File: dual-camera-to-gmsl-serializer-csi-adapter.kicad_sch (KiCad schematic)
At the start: 120 parts, among them J1 Conn_FFC_WE_68715014022, J2 Conn_FFC_WE_68715014022, J3 Conn_FFC_WE_68715014022, U1 TPS2117DRLR, U2 TPS2117DRLR, U3 AP62301_TSOT

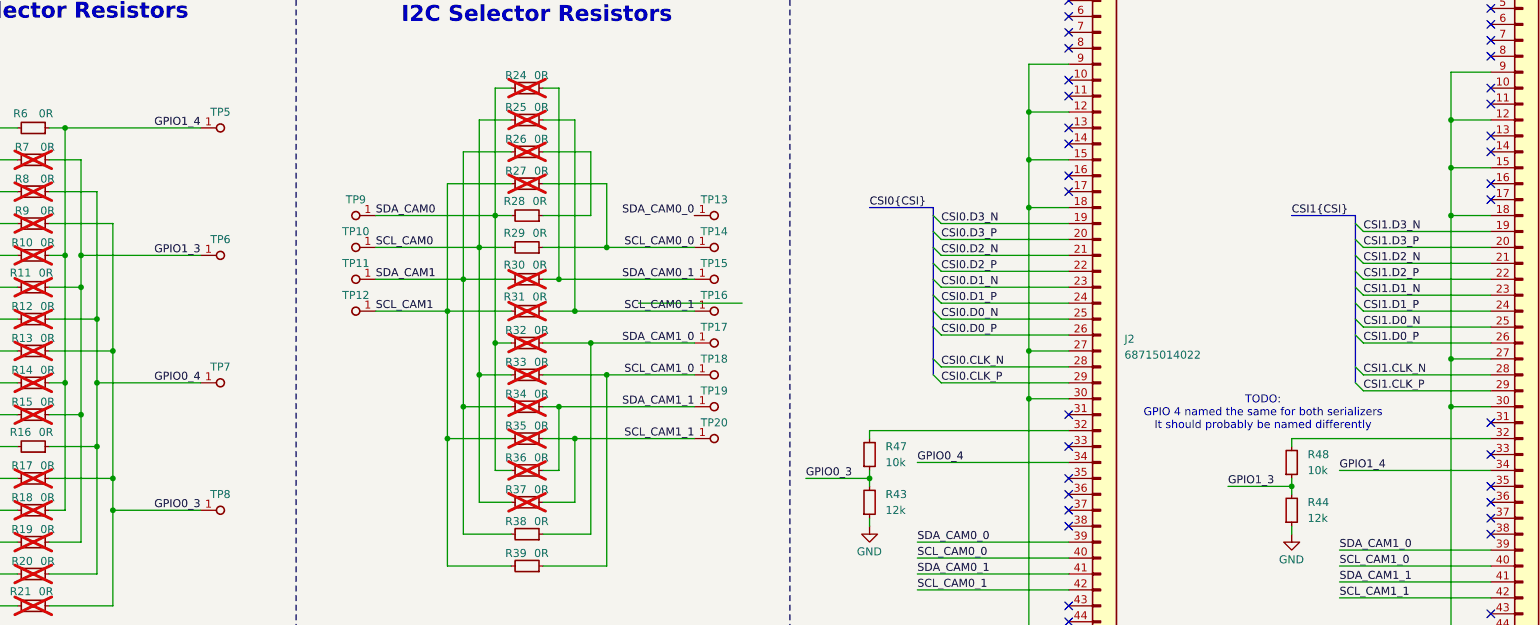
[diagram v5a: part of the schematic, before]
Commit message: [#70359] Schematic: Resolve GPIO naming
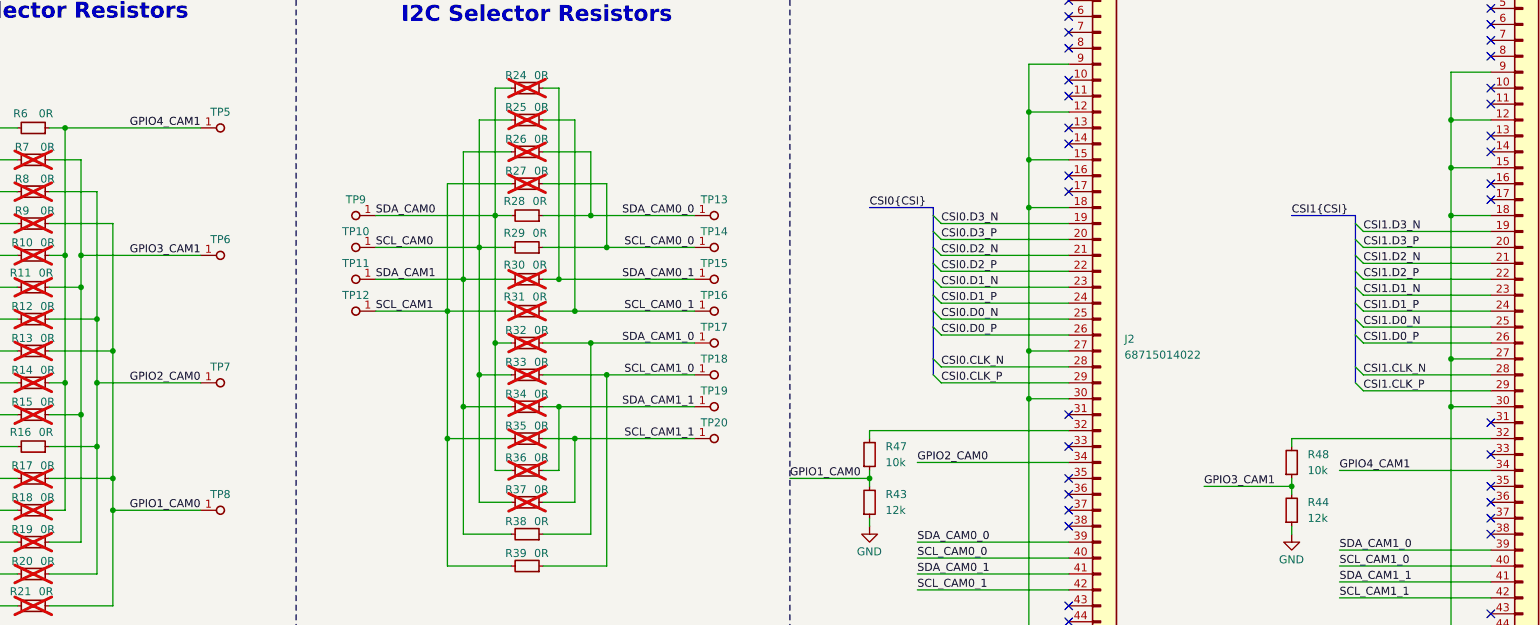
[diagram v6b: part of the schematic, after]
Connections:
- net SDA_CAM0_0: now also R26.1, R28.1
- net GPIO0_3 renamed GPIO1_CAM0
- net GPIO0_4 renamed GPIO2_CAM0
- net GPIO1_3 renamed GPIO3_CAM1
- net GPIO1_4 renamed GPIO4_CAM1
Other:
- note removed: "TODO: GPIO 4 named the same for both serializers It should probably be named differently"
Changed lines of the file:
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@@
 	)
 	(junction
+		(at 228.6 83.82)
+		(diameter 0)
+		(color 0 0 0 0)
+	)
+	(junction
 		(at 204.47 233.68)
 		(diameter 0)
@@
 	(wire
 		(pts
-			(xy 236.22 97.79) (xy 252.73 97.79)
+			(xy 228.6 83.82) (xy 245.11 83.82)
 		)
 		(stroke
@@
 	(wire
 		(pts
-			(xy 262.89 125.73) (xy 273.05 125.73)
+			(xy 260.35 125.73) (xy 273.05 125.73)
 		)
 		(stroke
@@
 	(wire
 		(pts
-			(xy 330.2 127) (xy 340.36 127)
+			(xy 326.39 127) (xy 340.36 127)
 		)
 		(stroke
@@
 		)
 	)
-	(text "TODO:\nGPIO 4 named the same for both serializers\nIt should probably be named differently"
-		(exclude_from_sim no)
-		(at 335.788 115.316 0)
-		(effects
-			(font
-				(size 1.27 1.27)
-			)
-		)
-	)
 	(text "CAM1"
 		(exclude_from_sim no)
@@
 		)
 	)
-	(label "GPIO1_4"
+	(label "GPIO4_CAM1"
 		(at 166.37 69.85 180)
 		(fields_autoplaced yes)
@@
 		)
 	)
-	(label "GPIO1_4"
+	(label "GPIO4_CAM1"
 		(at 347.98 124.46 0)
 		(fields_autoplaced yes)
@@
 		)
 	)
-	(label "GPIO0_4"
+	(label "GPIO2_CAM0"
 		(at 280.67 123.19 0)
 		(fields_autoplaced yes)
@@
 		)
 	)
-	(label "GPIO0_4"
+	(label "GPIO2_CAM0"
 		(at 166.37 110.49 180)
 		(fields_autoplaced yes)
@@
 		)
 	)
-	(label "GPIO0_3"
+	(label "GPIO1_CAM0"
 		(at 166.37 130.81 180)
 		(fields_autoplaced yes)
@@
 		)
 	)
-	(label "GPIO0_3"
-		(at 262.89 125.73 0)
+	(label "GPIO1_CAM0"
+		(at 260.35 125.73 0)
 		(fields_autoplaced yes)
 		(effects
@@
 		)
 	)
-	(label "GPIO1_3"
-		(at 330.2 127 0)
+	(label "GPIO3_CAM1"
+		(at 326.39 127 0)
 		(fields_autoplaced yes)
 		(effects
@@
 		)
 	)
-	(label "GPIO1_3"
+	(label "GPIO3_CAM1"
 		(at 166.37 90.17 180)
 		(fields_autoplaced yes)

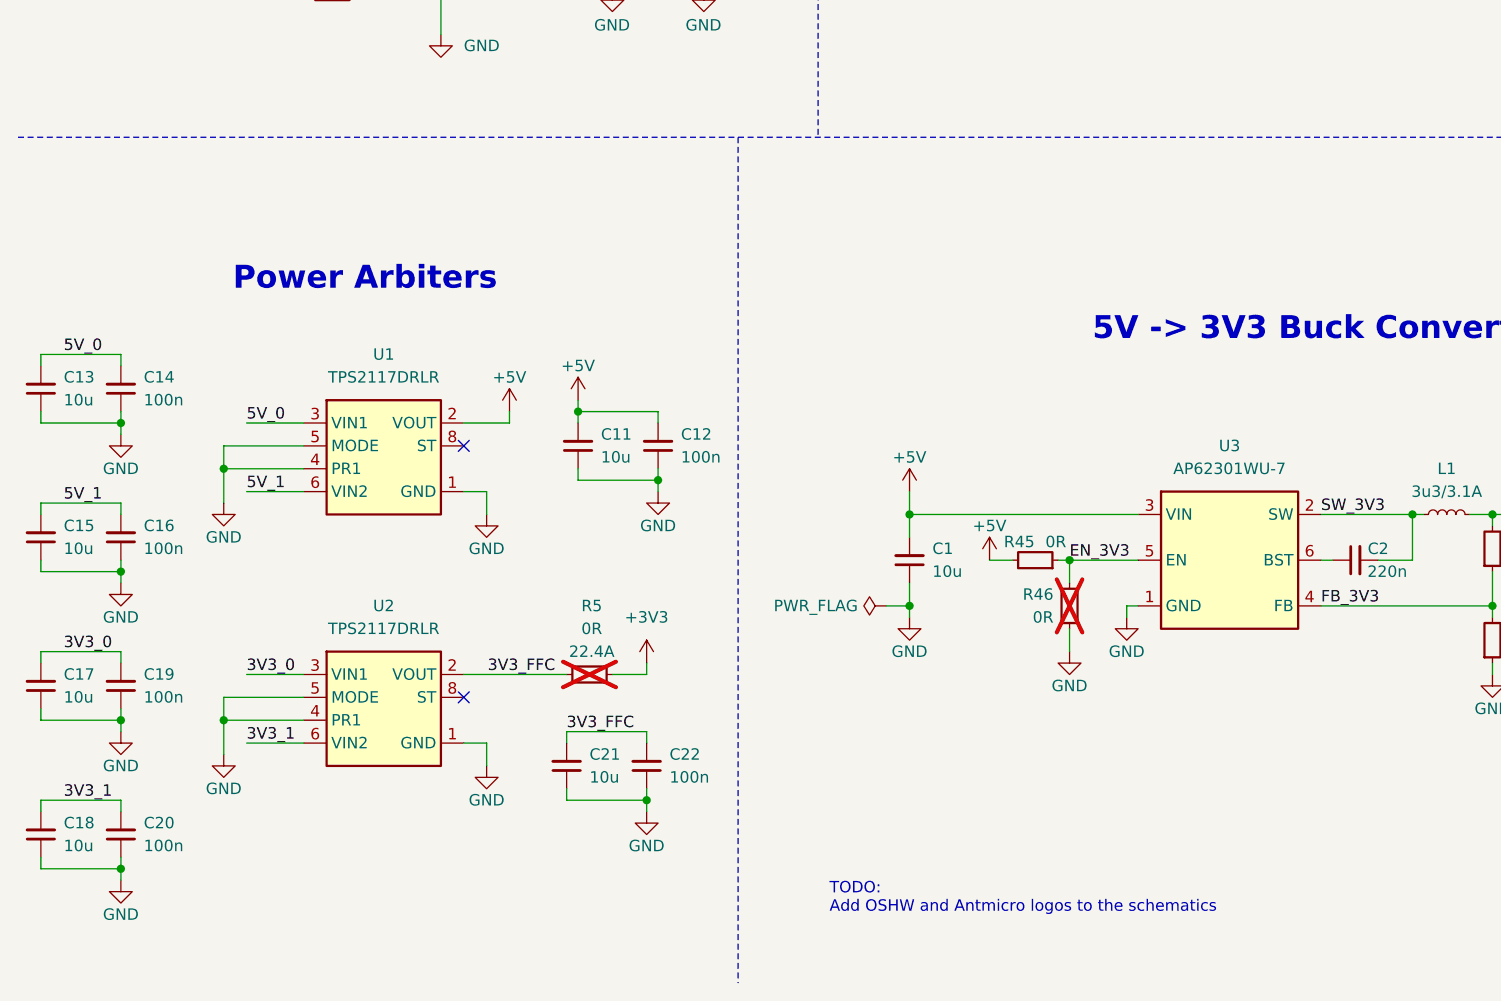
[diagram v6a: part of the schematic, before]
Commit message: [#70359] Schematic: Add OSHW & Antmicro logos
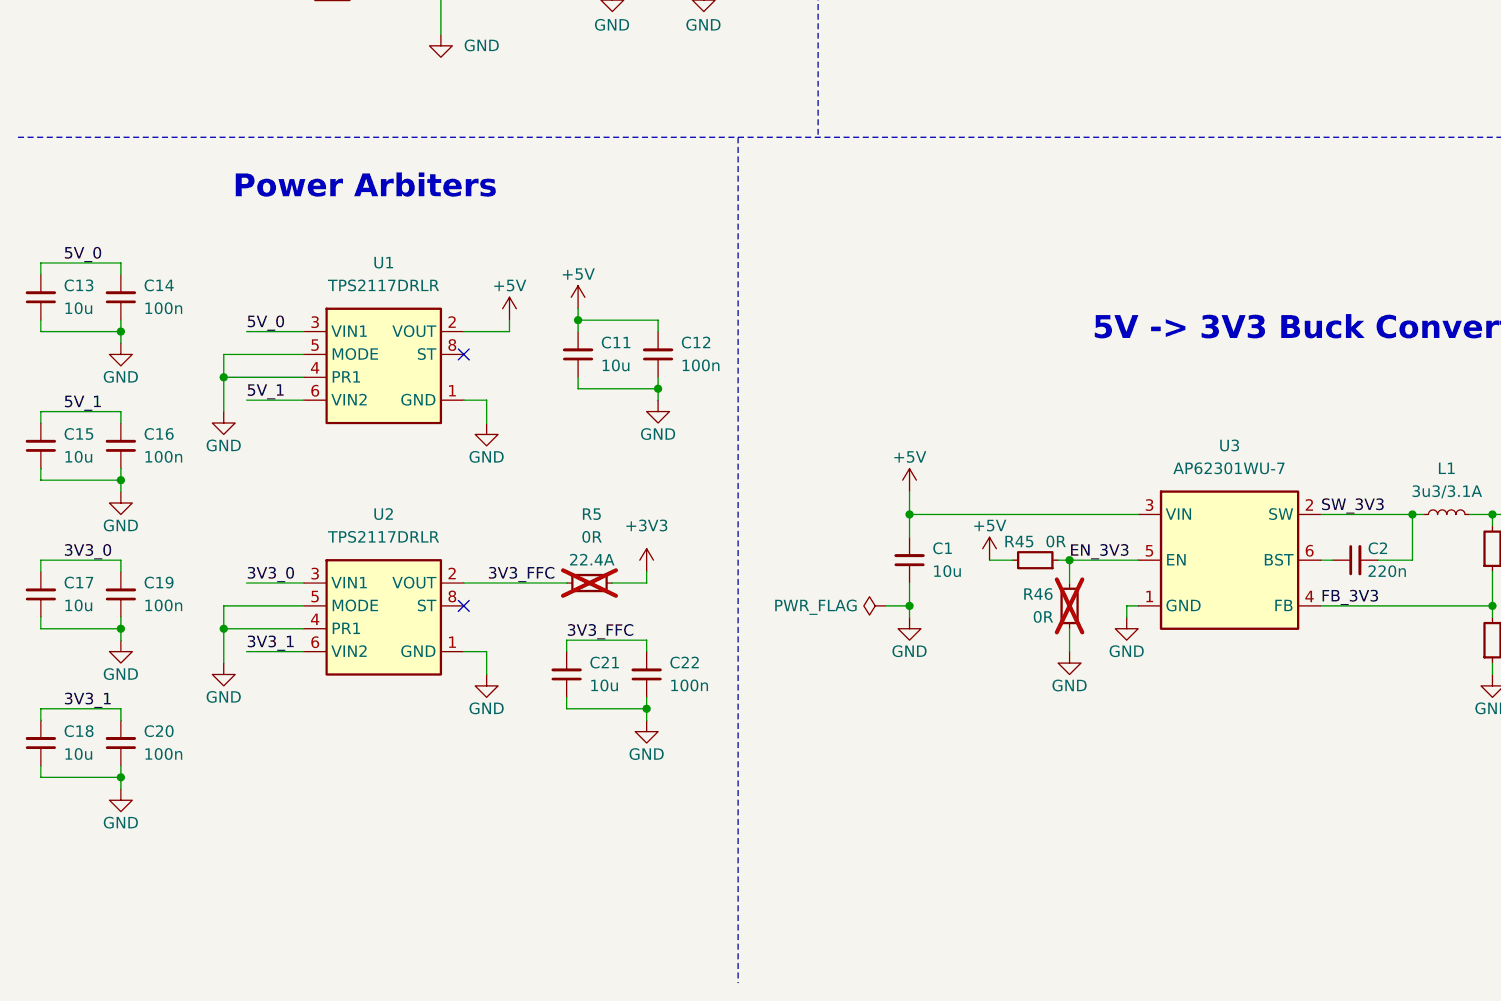
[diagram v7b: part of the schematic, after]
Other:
- note removed: "TODO: Add OSHW and Antmicro logos to the schematics"
- moved on the sheet: C11, C12, C13, C14, C15, C16, C17, C18, C19, C20, C21, C22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

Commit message: [#70359] Schematic: Add I2C Qwiic connectors
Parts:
- added C23, C24: C_100n_0402, antmicro-footprints:C_0402_1005Metric, symbol antmicroCapacitors0402:C_100n_0402
- added D7, D8: ESD9X5.0ST5G, antmicro-footprints:SOD-923, symbol antmicroTVSDiodes:ESD9X5.0ST5G
- added J4, J5: JST_SH_1x4_SM04B-SRSS-TB-LF-SN, antmicro-footprints:Conn_JST_SH_1x4_SM04B-SRSS-TB-LF-SN, symbol antmicroWire2BoardConnectors:JST_SH_1x4_SM04B-SRSS-TB-LF-SN
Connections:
- net +3V3: now also C23.2, C24.2, D7.1 (C), D8.1 (C), J4.2, J5.2
- net GND: now also C23.1, C24.1, D7.2 (A), D8.2 (A), J4.1, J5.1
- net SCL_CAM0: now also J4.4
- net SCL_CAM1: now also J5.4
- net SDA_CAM0: now also J4.3
- net SDA_CAM1: now also J5.3
- no-connect marks 62 -> 64
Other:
- note removed: "TODO: Add QWIC connectors for I2C exposed from every serializer This will allow to add more sensors and stream sensor data over GMSL"
- moved on the sheet: R10, R11, R12, R13, R14, R15, R16, R17, R18, R19, R20, R21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
